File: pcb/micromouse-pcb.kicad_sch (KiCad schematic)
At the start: 43 parts, among them J1 Conn_01x08, J1_MotorEncoder1 Conn_01x06, J2 Conn_01x08, J2_MotorEncoder1 Conn_01x06, Q1 FQP27P06, SW3 SW_SPDT, SW4 SW_Push, SW5 SW_Push, U1 Teensy_4.1, U2 AP63205WU, U3 LSM6DSV16XTR

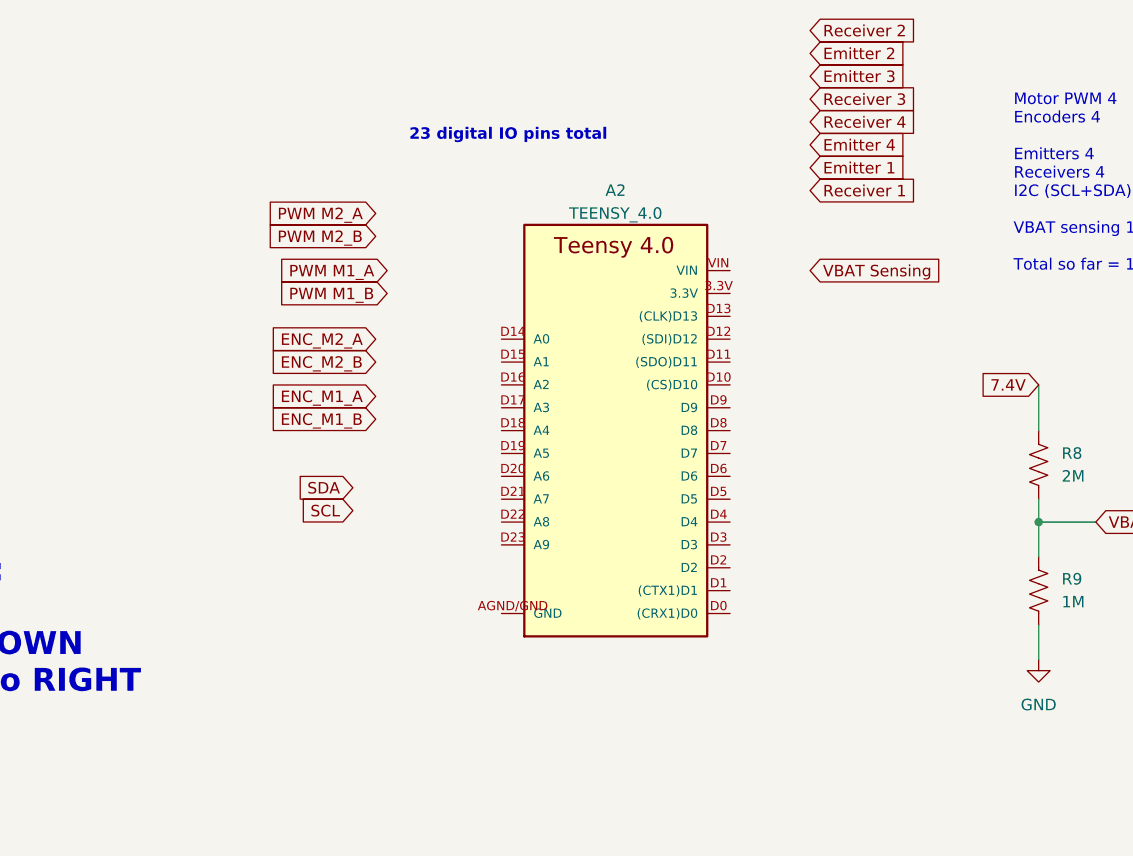
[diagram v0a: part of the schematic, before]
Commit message: connected pins to microcontroller and switched footprint for encoders
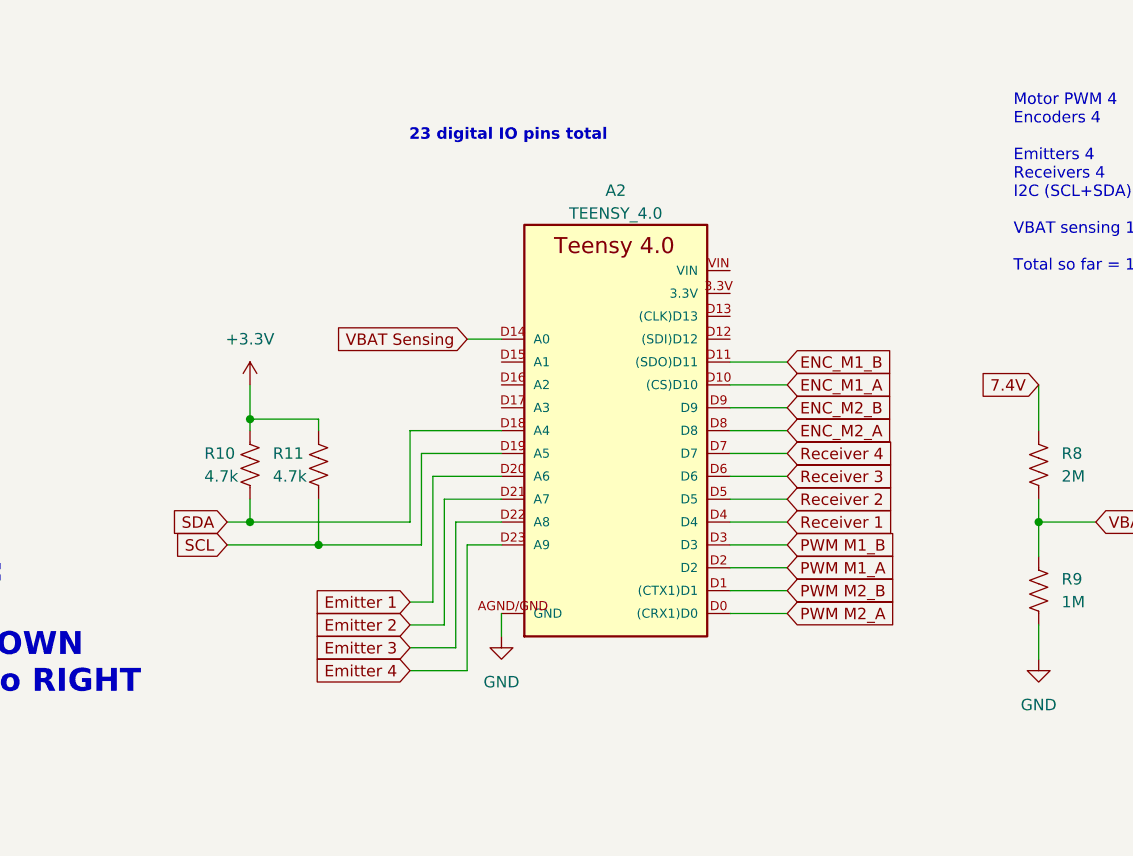
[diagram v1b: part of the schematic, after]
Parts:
- added R10, R11: 4.7k, Resistor_SMD:R_0603_1608Metric_Pad0.98x0.95mm_HandSolder, symbol Device:R_US
- J1_MotorEncoder1, J2_MotorEncoder1: footprint Connector_PinSocket_2.54mm:PinSocket_1x06_P2.54mm_Vertical -> Connector_JST:JST_SH_BM06B-SRSS-TB_1x06-1MP_P1.00mm_Vertical
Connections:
- net +3.3V: now also R10.1, R11.1
- net ENC_M1_A: now also A2.D10 ((CS)D10)
- net ENC_M1_B: now also A2.D11 ((SDO)D11)
- net ENC_M2_A: now also A2.D8
- net ENC_M2_B: now also A2.D9
- net Emitter 1: now also A2.D20 (A6)
- net Emitter 2: now also A2.D21 (A7)
- net Emitter 3: now also A2.D22 (A8)
- net Emitter 4: now also A2.D23 (A9)
- net PWM M1_A: now also A2.D2
- net PWM M1_B: now also A2.D3
- net PWM M2_A: now also A2.D0 ((CRX1)D0)
- net PWM M2_B: now also A2.D1 ((CTX1)D1)
- net Receiver 1: now also A2.D4
- net Receiver 2: now also A2.D5
- net Receiver 3: now also A2.D6
- net Receiver 4: now also A2.D7
- net SCL: now also A2.D19 (A5), R11.2
- net SDA: now also A2.D18 (A4), R10.2
- net VBAT Sensing: now also A2.D14 (A0)

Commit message: initial layout
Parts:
- removed D1: LED, LED_SMD:LED_1206_3216Metric_Pad1.42x1.75mm_HandSolder, symbol Device:LED
- removed R1, R3: 10k, Resistor_SMD:R_0603_1608Metric_Pad0.98x0.95mm_HandSolder, symbol Device:R_US
- removed R4: 1k, Resistor_SMD:R_0603_1608Metric_Pad0.98x0.95mm_HandSolder, symbol Device:R_US
- removed R6, R7: 4.7k, Resistor_SMD:R_0603_1608Metric_Pad0.98x0.95mm_HandSolder, symbol Device:R_US
- removed SW4, SW5: SW_Push, Button_Switch_SMD:SW_SPST_TL3342, symbol Switch:SW_Push
- removed TP3, TP4, TP6: TestPoint, Ratatouii:TestPoint_THTPad_D2.0mm_Drill1.0mm, symbol Connector:TestPoint
- removed U1: Teensy_4.1, Ratatouii:Teensy4.1_LessHoles, symbol micromouse-symbols:Teensy_4.1
- added D2: LED, LED_SMD:LED_1206_3216Metric_Pad1.42x1.75mm_HandSolder, symbol Device:LED
- added H7: MountingHole, MountingHole:MountingHole_2.2mm_M2, symbol Mechanical:MountingHole
- added R12: 1k, Resistor_SMD:R_0603_1608Metric_Pad0.98x0.95mm_HandSolder, symbol Device:R_US
- added R13: 10k, Resistor_SMD:R_0603_1608Metric_Pad0.98x0.95mm_HandSolder, symbol Device:R_US
- added SW6: SW_Push, Button_Switch_SMD:SW_SPST_TL3342, symbol Switch:SW_Push
- added U4: DRV8833PW, Package_SO:TSSOP-16_4.4x5mm_P0.65mm, symbol Driver_Motor:DRV8833PW
- L1: footprint Inductor_SMD:L_1812_4532Metric_Pad1.30x3.40mm_HandSolder -> Inductor_SMD:L_1008_2520Metric_Pad1.43x2.20mm_HandSolder
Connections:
- net +3.3V: now also A2.3.3V, R13.1
- net GND: now also D2.1 (K), SW6.2
- net PWMA_6612: no longer names the net of J2.1 (Pin_1)
- net PWMB_6612: no longer names the net of J2.7 (Pin_7)
- new net: D2.2 (A), R12.1
- new net: R13.2, SW6.1
- no-connect marks 21 -> 4
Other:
- moved on the sheet: A2, R10, R11

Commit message: drv8833 schematic; layout component groupingi
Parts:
- removed J1, J2: Conn_01x08, Connector_PinSocket_2.54mm:PinSocket_1x08_P2.54mm_Vertical, symbol Connector_Generic:Conn_01x08
- added C10: 0.01uF >16V, Capacitor_SMD:C_0603_1608Metric_Pad1.08x0.95mm_HandSolder, symbol Device:C
- added C8: C 2.2uF 6.3V, Capacitor_SMD:C_0603_1608Metric_Pad1.08x0.95mm_HandSolder, symbol Device:C
- added C9: C 47uF >10V, Capacitor_SMD:C_1206_3216Metric_Pad1.33x1.80mm_HandSolder, symbol Device:C
- added TP6: TestPoint, Ratatouii:TestPoint_THTPad_D2.0mm_Drill1.0mm, symbol Connector:TestPoint
- D2: footprint LED_SMD:LED_1206_3216Metric_Pad1.42x1.75mm_HandSolder -> LED_SMD:LED_0603_1608Metric_Pad1.05x0.95mm_HandSolder
- R12: value 1k -> 4.7k
- SW6: footprint Button_Switch_SMD:SW_SPST_TL3342 -> Ratatouii:SW-SMD_L4.0-W2.9-LS5.0
- U4: footprint Package_SO:TSSOP-16_4.4x5mm_P0.65mm -> Package_SO:TSSOP-16-1EP_4.4x5mm_P0.65mm_EP3x3mm_ThermalVias
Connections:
- net POW_M1_A is gone; now on net Motor L Power 1: J1_MotorEncoder1.5 (Pin_5)
- net POW_M1_B is gone; now on net Motor L Power 2: J1_MotorEncoder1.6 (Pin_6)
- net POW_M2_A is gone; now on net Motor R Power 1: J2_MotorEncoder1.5 (Pin_5)
- net POW_M2_B is gone; now on net Motor R Power 2: J2_MotorEncoder1.6 (Pin_6)
- net PWM M1_A is gone; now on net Motor L Logic 1: A2.D2
- net PWM M1_B is gone; now on net Motor L Logic 2: A2.D3
- net PWM M2_A is gone; now on net Motor R Logic 1: A2.D0 ((CRX1)D0)
- net PWM M2_B is gone; now on net Motor R Logic 2: A2.D1 ((CTX1)D1)
- net +3.3V: now also U4.1 (~{SLEEP})
- net +5V: now also A2.VIN, R12.2
- net 7.4V: now also U4.12 (VM), C10.2, C9.1, TP6.1
- net GND: now also U4.13 (GND), U4.3 (AISEN), U4.6 (BISEN), C8.2, C9.2
- net Gooo button: now reaches R13.2, SW6.1
- net Gooo button: now also A2.D12 ((SDI)D12)
- net Motor L Logic 2: now reaches U4.10 (BIN2)
- net at U4.11 (VCP): now also C10.1
- net at U4.14 (VINT): now also C8.1
- net Motor R Logic 2: now reaches U4.15 (AIN2)
- net Motor R Logic 1: now reaches U4.16 (AIN1)
- net Motor R Power 1: now reaches U4.2 (AOUT1)
- net Motor R Power 2: now reaches U4.4 (AOUT2)
- net Motor L Power 2: now reaches U4.5 (BOUT2)
- net Motor L Power 1: now reaches U4.7 (BOUT1)
- net Motor L Logic 1: now reaches U4.9 (BIN1)
- net ENC_M1_A renamed Encoder L A
- net ENC_M1_B renamed Encoder L B
- net ENC_M2_A renamed Encoder R A
- net ENC_M2_B renamed Encoder R B
- no-connect marks 4 -> 9
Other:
- note added: "Bulk Capacitor"
- note added: "Encoder Connectors"
- note added: "Internal supply bypass(filtering) capacitor"
- note added: "Misc"
- note added: "Switched naming Scheme: Motors - Left/Right motor Inputs 1 and 2 (A/B and 1/2 can be confusing)"
- note removed: "Motors With Encoders"
- note removed: "Note: The pins labeled PWM6612 are for compatibility with the TB6612FNG H-bridge. When choosing TB6612FNG, solder a jumper wire from the pin to 3.3V through the test points."
- moved on the sheet: D2, H1, H2, H3, H4, H5, H6, H7, R10, R11, R12, R8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
